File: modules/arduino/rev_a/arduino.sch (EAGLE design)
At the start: 45 parts, among them IC5 ATMEGA328P-20MU, J1 MODULE_GENERIC, J4 MICRO_USB_B_HIROSE_ZX62-B-5PA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, U3 ATMEGA8U2-MU, Y1 12 MHz, Y2 16MHz

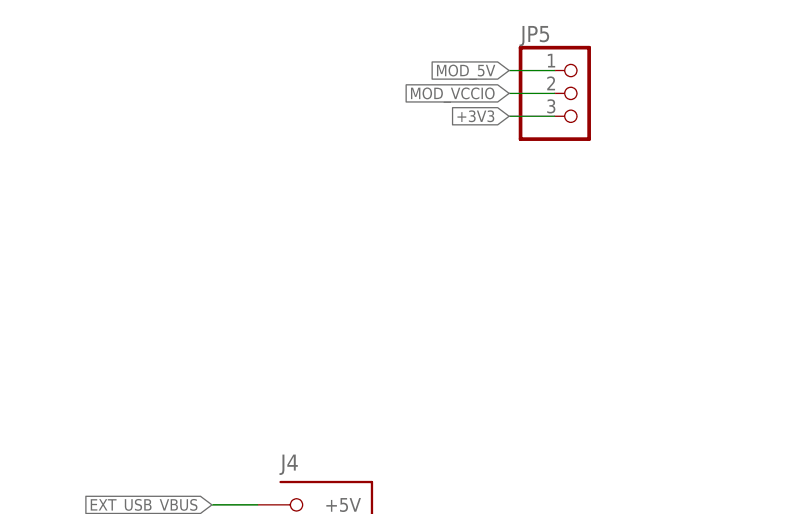
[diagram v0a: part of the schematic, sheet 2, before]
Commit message: Ardunio WIP
 - Add actual holes for signpost module mounts
 - Replace pin header with switch for IO voltage
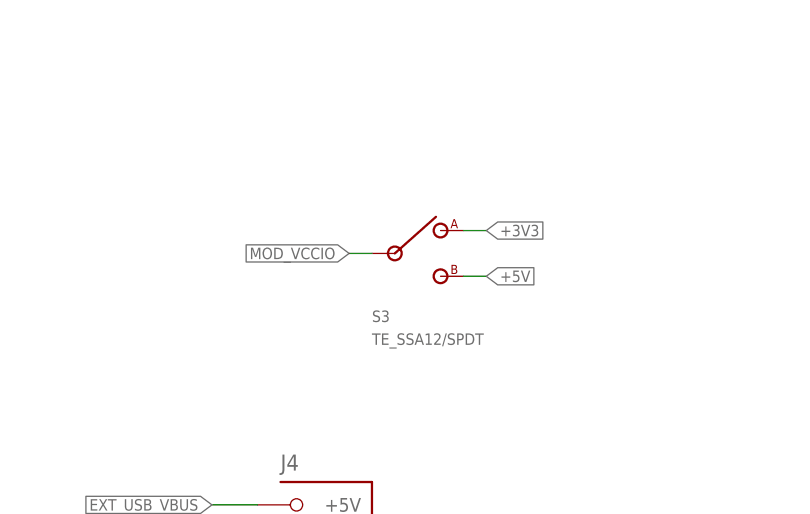
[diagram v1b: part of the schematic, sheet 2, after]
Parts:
- removed JP5: (no value), pinhead:PINHD-1X3
- added S3: TE_SSA12/SPDT, switches:TE_SSA12/SPDT
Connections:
- net +3V3: no longer JP5.3
- net +5V: now also S3.B
- net MOD_5V: no longer JP5.1
- net MOD_VCCIO: no longer JP5.2
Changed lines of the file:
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@@
 <part name="J1" library="signpost" deviceset="MODULE_GENERIC" device=""/>
 <part name="GND24" library="umich" deviceset="GND" device=""/>
-<part name="JP5" library="pinhead" deviceset="PINHD-1X3" device=""/>
 <part name="VR1" library="regulators" deviceset="TPS62086" device=""/>
 <part name="GND26" library="umich" deviceset="GND" device=""/>
@@
 <attribute name="DIGIKEY" value="535-9103-1-ND"/>
 </part>
+<part name="S3" library="switches" deviceset="TE_SSA12/SPDT" device=""/>
 </parts>
 <sheets>
@@
 <instance part="J1" gate="G$1" x="33.02" y="149.86"/>
 <instance part="GND24" gate="1" x="48.26" y="127"/>
-<instance part="JP5" gate="A" x="223.52" y="170.18"/>
 <instance part="VR1" gate="G$1" x="50.8" y="40.64"/>
 <instance part="GND26" gate="1" x="35.56" y="27.94"/>
@@
 <instance part="S1" gate="G$1" x="185.42" y="66.04"/>
 <instance part="GND28" gate="1" x="198.12" y="43.18"/>
+<instance part="S3" gate="G$1" x="203.2" y="152.4"/>
 </instances>
 <busses>
@@
 <net name="+3V3" class="0">
 <segment>
-<pinref part="JP5" gate="A" pin="3"/>
-<wire x1="215.9" y1="167.64" x2="220.98" y2="167.64" width="0.1524" layer="91"/>
-<label x="215.9" y="167.64" size="1.27" layer="95" rot="R180" xref="yes"/>
+<wire x1="213.36" y1="154.94" x2="210.82" y2="154.94" width="0.1524" layer="91"/>
+<label x="213.36" y="154.94" size="1.27" layer="95" xref="yes"/>
 </segment>
 <segment>
@@
 </segment>
 <segment>
-<pinref part="JP5" gate="A" pin="1"/>
-<wire x1="215.9" y1="172.72" x2="220.98" y2="172.72" width="0.1524" layer="91"/>
-<label x="215.9" y="172.72" size="1.27" layer="95" rot="R180" xref="yes"/>
-</segment>
-<segment>
 <pinref part="VR1" gate="G$1" pin="VIN"/>
 <wire x1="22.86" y1="45.72" x2="27.94" y2="45.72" width="0.1524" layer="91"/>
@@
 <net name="MOD_VCCIO" class="0">
 <segment>
-<pinref part="JP5" gate="A" pin="2"/>
-<wire x1="215.9" y1="170.18" x2="220.98" y2="170.18" width="0.1524" layer="91"/>
-<label x="215.9" y="170.18" size="1.27" layer="95" rot="R180" xref="yes"/>
+<wire x1="198.12" y1="152.4" x2="200.66" y2="152.4" width="0.1524" layer="91"/>
+<label x="198.12" y="152.4" size="1.27" layer="95" rot="R180" xref="yes"/>
 </segment>
 <segment>
@@
 <pinref part="D2" gate="G$1" pin="CATHODE"/>
 </segment>
-</net>
+<segment>
+<pinref part="S3" gate="G$1" pin="B"/>
+<wire x1="213.36" y1="149.86" x2="210.82" y2="149.86" width="0.1524" layer="91"/>
+<label x="213.36" y="149.86" size="1.27" layer="95" xref="yes"/>
+</segment>
+</net>

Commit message: Add Digikey attributes for Arduino MCUs
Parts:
- IC5: DIGIKEY (none) -> ATMEGA328P-MU-ND
- U3: DIGIKEY (none) -> ATMEGA8U2-MURCT-ND
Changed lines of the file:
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@@
 <part name="L" library="led" deviceset="LED" device="CHIP-LED0805" value="YELLOW"/>
 <part name="GND17" library="supply1" deviceset="GND" device=""/>
-<part name="U3" library="atmel" deviceset="ATMEGA8U2-MU" device=""/>
+<part name="U3" library="atmel" deviceset="ATMEGA8U2-MU" device="">
+<attribute name="DIGIKEY" value="ATMEGA8U2-MURCT-ND"/>
+</part>
 <part name="C5" library="SmartPrj" deviceset="C-EU" device="0603-RND" value="100n"/>
 <part name="ICSP1" library="pinhead" deviceset="PINHD-2X3" device="" value="ICSP"/>
@@
 <part name="GND8" library="supply1" deviceset="GND" device=""/>
 <part name="JP2" library="pinhead" deviceset="PINHD-2X2" device=""/>
-<part name="IC5" library="idii" deviceset="MEGA8" device="-MI" value="ATMEGA328P-20MU"/>
+<part name="IC5" library="idii" deviceset="MEGA8" device="-MI" value="ATMEGA328P-20MU">
+<attribute name="DIGIKEY" value="ATMEGA328P-MU-ND"/>
+</part>
 <part name="GND15" library="supply1" deviceset="GND" device=""/>
 <part name="FRAME1" library="lab11-frames" deviceset="LETTER_L_UMICH" device=""/>
@@
 <instance part="L" gate="G$1" x="287.02" y="116.84" rot="R90"/>
 <instance part="GND17" gate="1" x="299.72" y="116.84" rot="R90"/>
-<instance part="U3" gate="G$1" x="119.38" y="53.34"/>
+<instance part="U3" gate="G$1" x="119.38" y="53.34">
+<attribute name="DIGIKEY" x="119.38" y="53.34" size="1.27" layer="96" align="top-left" display="off"/>
+</instance>
 <instance part="C5" gate="G$1" x="180.34" y="81.28" rot="R90"/>
 <instance part="ICSP1" gate="A" x="60.96" y="99.06"/>
@@
 <attribute name="NAME" x="217.17" y="76.835" size="1.778" layer="95"/>
 <attribute name="VALUE" x="217.805" y="14.605" size="1.778" layer="96"/>
+<attribute name="DIGIKEY" x="233.68" y="48.26" size="1.27" layer="96" align="top-left" display="off"/>
 </instance>
 <instance part="GND15" gate="1" x="167.64" y="45.72"/>

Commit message: Not pretty but it's something
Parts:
- removed L1: BLM21, wuerth-elektronik:WE-CBF_0805
- removed Z1, Z2: PGB1010604, varistor:VARISTORCN0603
- added D1: DIODE, passives:DIODE
- added J2: (no value), jumper:SJ
- added LOGO1: UMICH_SOLID_MEDIUM, logos:UMICH_SOLID_MEDIUM
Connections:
- net N$7 renamed VR_IND_SW
- removed net USHIELD: L1.2, Z1.2, Z2.2
- net +3V3: now also S3.A
- net +5V: now also C10.1, D1.CATHODE, VR1.EN, VR1.VIN
- net ARD_USB_D+: now also RN3B.2; no longer RN3D.2, Z1.1
- net ARD_USB_D-: no longer Z2.1
- net ARD_USB_GND: no longer GROUND.2, L1.1
- net ARD_USB_VBUS: no longer D2.ANODE
- net EXT_USB_GND: now also GROUND.1
- net EXT_USB_VBUS: now also D2.ANODE
- net GND: now also GROUND.2; no longer GROUND.1
- net MOD_5V: now also D1.ANODE; no longer C10.1, VR1.EN, VR1.VIN
- net MOD_IN: now also J2.1
- net MOD_VCCIO: now also S3.IN
- net RD+: now also RN3B.1; no longer RN3D.1
- net RESET: now also J2.2
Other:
- note added: "RN3D to RN3B (routing)"
- note added: "Remove shield ESD circuitry"
- moved on the sheet: D2, RN3B, RN3D

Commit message: Arduino: WIP, I should commit more frequently :(
The primary change in this commit is to extend the 3.3V/5V selection to the whole
board. The nice observation is that the two MCUs are 2.7-5.5 and 1.8-5.5 VCC tolerant,
so can do run-time selection of core voltage with a little bit of careful design. This
lets the seinduino look either like a Due (3.3V) or a Uno (5V).

The next mission is to replace that reset trigger circuit with a one-shot so that we
aren't cooking 5mA all the time.
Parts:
- removed ICSP1: ICSP, pinhead:PINHD-2X3
- removed RN3: 22R, resistor-dil:4R-NCAY16
- added C1, C13, C2, C3: 100nF, passives:CAPACITOR0603_CAP
- added J3: ICSP_PROG, pinhead:PINHD-2X3
- added JP1: (no value), pinhead:PINHD-1X2
- added R4, R5: 22Ω, passives:RESISTOR-HIGH_SPEED0402
- added U1, U2: ADG3304, chips:ADG3304
- C7: value 100n -> 100nF
- C8: value 1u -> 1uF
- renumbered IC5 to U4, ICSP to J6, JP2 to J5
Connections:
- removed net EXT_USB_ID: J4.ID
- removed net MISO2: ICSP1.1, U3.(PD0/MISO/PCINT3)PB3
- removed net MOD_VCCIO: J1.VCCIO, S3.IN
- removed net MOSI2: ICSP1.4, U3.(PDI/MOSI/PCINT2)PB2
- removed net RD+: RN3B.1, U3.D+
- removed net RD-: RN3A.1, U3.D-
- removed net RESET2: ICSP1.5, RN1C.2, U3.RESET(PC1/DW)
- removed net SCK2: ICSP1.3, U3.(SCLK/PCINT1)PB1
- new net ARD_USB_D+_TERM: R5.P$1, U3.D+
- new net ARD_USB_D-_TERM: R4.P$1, U3.D-
- new net MISO_PROG: U1.A1, U3.(PD0/MISO/PCINT3)PB3
- new net MISO_PROG_SHIFTED: J3.1, U1.Y1
- new net MISO_SHIFTED: J6.1, U2.Y1
- new net MOSI_PROG: U1.A2, U3.(PDI/MOSI/PCINT2)PB2
- new net MOSI_PROG_SHIFTED: J3.4, U1.Y2
- new net MOSI_SHIFTED: J6.4, U2.Y2
- new net RESET_PROG: RN1C.2, U1.A4, U3.RESET(PC1/DW)
- new net RESET_PROG_SHIFTED: J3.5, U1.Y4
- new net RESET_SHIFTED: J6.5, U2.Y4
- new net SCK_PROG: U1.A3, U3.(SCLK/PCINT1)PB1
- new net SCK_PROG_SHIFTED: J3.3, U1.Y3
- new net SCK_SHIFTED: J6.3, U2.Y3
- new net VCC: C13.2, C2.2, C6.2, C7.1, J1.VCCIO, RN1C.1, RN1D.2, S3.IN, U1.EN, U1.VCC_A, U2.EN, U2.VCC_A, U3.AVCC, U3.VCC, U4.AVCC, U4.VCC@1, U4.VCC@2
- net +5V: now also C1.1, C3.1, J3.2, U1.VCC_Y, U2.VCC_Y; no longer C6.2, C7.1, ICSP1.2, RN1C.1, RN1D.2, U3.AVCC, U3.VCC, U4.AVCC, U4.VCC@1, U4.VCC@2
- net AD4: now also JP1.2
- net AD5: now also JP1.1
- net ARD_USB_D+: now also R5.P$2; no longer RN3B.2
- net ARD_USB_D-: now also R4.P$2; no longer RN3A.2
- net GND: now also C1.2, C13.1, C2.1, C3.2, J3.6, U1.GND, U2.GND; no longer ICSP1.6
- net MISO: now also U2.A1; no longer J6.1
- net MOSI: now also U2.A2; no longer J6.4
- net RESET: now also U2.A4; no longer J6.5
- net SCK: now also U2.A3; no longer J6.3
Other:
- note added: "AD4 = SDA"
- note added: "AD5 = SCL"
- note added: "Add missing extra SCL/SDA headers"
- note added: "Cautionary level conversion on the programming headers"
- note added: "Other Stuff:"
- note added: "Rename parts consistently"
- note added: "Replace RN3 array with discretes"
- note added: "Replace nets with labels where I just couldn't stand it any more"
- note added: "Update design to support either 3.3 or 5V for VCC"
- note added: "VCC Selection - Chooses core voltage for all MCUs - Chooses I/O voltage for all I/O lines - NOTE: Arduino ICSP header is always at +5V regardless of selection - Should match Due at 3.3V and Uno at 5V"
- note added: "http://forum.arduino.cc/index.php?topic=136595.0"
- note removed: "RN3D to RN3B (routing)"
- moved on the sheet: C4, C7, C8, F1, L, ON, POWER, RN1C, RN1D, RN2A, RN4C, RN4D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

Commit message: arudino: add reset network
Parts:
- removed J2, RESET-EN: (no value), jumper:SJ
- added C14, C15: 100nF, passives:CAPACITOR0603_CAP
- added R6: 10kΩ, passives:RESISTOR0603_RES
- added RESET-PROG-EN, RESET-SIGN-EN: (no value), jumper:SJ
- added U5: 74LVC2G00DC, chips:74LVC2G00DC
- added U6: SN74LVC1G123DCUR, chips:SN74LVC1G123DCUR
- C5: value 100n -> 100nF; device SmartPrj:C-EU0603-RND -> passives:CAPACITOR0603_CAP
- RN1: DIGIKEY (none) -> CAY16-103J4GLFCT-ND
- RN3: DIGIKEY (none) -> CAY16-102J4GLFCT-ND
- renumbered RN4 to RN3
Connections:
- removed net DTR: C5.1, RN2D.1, U3.(CTS/HWB/AIN6/TO/INT7)PD7
- new net DTR_PROG: RESET-PROG-EN.1, U3.(CTS/HWB/AIN6/TO/INT7)PD7
- new net N$10: RESET-SIGN-EN.2, RN1B.2, U5G$1.B
- new net N$13: U5G$2.A, U5G$2.B, U6.Q
- new net N$7: C5.2, RN1C.1, U6.C_EX
- new net N$8: U5G$1.Y, U6.!A
- new net N$9: RESET-PROG-EN.2, RN1A.2, U5G$1.A
- net GND: now also C14.1, C15.1, RN1C.2, U5G$3.GND, U6.GND; no longer RN2D.2
- net MOD_IN: now also RESET-SIGN-EN.1; no longer J2.1
- net RESET: now also RN1D.2, U5G$2.Y; no longer C5.2, J2.2, RESET-EN.1, RESET-EN.2, RN1D.1
- net RESET_PROG: now also R6.1; no longer RN1C.2
- net VCC: now also C14.2, C15.2, C5.1, R6.2, RN1A.1, RN1B.1, RN1D.1, U5G$3.VCC, U6.!CLR, U6.B, U6.R/C_EX, U6.VCC; no longer RN1C.1, RN1D.2
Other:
- note added: "1 ms pulse"
- note added: "Arduino uses serial DTR to trigger reset, with semantics of falling edge on DTR line results in negative pulse for reset"
- note added: "Replace reset (see right)"
- note added: "Reset Network"
- moved on the sheet: RN1C, RN1D

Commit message: Seinduino routed
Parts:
- removed RN2, RN3: 1K, resistor-dil:4R-NCAY16
- added C16: 100nF, passives:CAPACITOR0603_CAP
- added R10, R11, R12, R7, R8: 1kΩ, passives:RESISTOR0603_RES
- added R9: 470Ω, passives:RESISTOR0603_RES
- C4, C6: value 100n -> 100nF; device SmartPrj:C-EU0603-RND -> passives:CAPACITOR0603_CAP
- C7: device SmartPrj:C-EU0603-RND -> passives:CAPACITOR0603_CAP
- U1: value ADG3304 -> ATMEGA8U2-MU; device chips:ADG3304 -> atmel:ATMEGA8U2-MU; DIGIKEY (none) -> ATMEGA8U2-MURCT-ND
- U2: value ADG3304 -> ATMEGA328P-20MU; device chips:ADG3304 -> idii:MEGA8-MI; DIGIKEY (none) -> ATMEGA328P-MU-ND
- U3: value ATMEGA8U2-MU -> ADG3304; device atmel:ATMEGA8U2-MU -> chips:ADG3304; DIGIKEY ATMEGA8U2-MURCT-ND -> (none)
- U4: value ATMEGA328P-20MU -> ADG3304; device idii:MEGA8-MI -> chips:ADG3304; DIGIKEY ATMEGA328P-MU-ND -> (none)
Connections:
- removed net N$10: RESET-SIGN-EN.2, RN1B.2, U5G$1.B
- removed net N$9: RESET-PROG-EN.2, RN1A.2, U5G$1.A
- net +5V: now also R7.2, R8.2, R9.1, U3.VCC_Y, U4.VCC_Y; no longer RN2B.1, RN2C.1, RN3C.1, RN3D.1, U1.VCC_Y, U2.VCC_Y
- net AD0: now also U2.PC0(ADC0); no longer U4.PC0(ADC0)
- net AD1: now also U2.PC1(ADC1); no longer U4.PC1(ADC1)
- net AD2: now also U2.PC2(ADC2); no longer U4.PC2(ADC2)
- net AD3: now also U2.PC3(ADC3); no longer U4.PC3(ADC3)
- net AD4: now also U2.PC4(ADC4/SDA); no longer U4.PC4(ADC4/SDA)
- net AD5: now also U2.PC5(ADC5/SCL); no longer U4.PC5(ADC5/SCL)
- net ARD_USB_D+_TERM: now also U1.D+; no longer U3.D+
- net ARD_USB_D-_TERM: now also U1.D-; no longer U3.D-
- net ARD_USB_GND: now also U1.UGND; no longer U3.UGND
- net AREF: now also U2.AREF; no longer U4.AREF
- net DTR_PROG: now also RESET-PROG-EN.2, RN1A.2, U1.(CTS/HWB/AIN6/TO/INT7)PD7, U5G$1.A; no longer U3.(CTS/HWB/AIN6/TO/INT7)PD7
- net GND: now also C16.2, C6.2, RN1D.2, U1.PAD, U2.AGND, U2.GND@1, U2.GND@2, U4.GND; no longer C6.1, RN1C.2, U2.GND, U3.PAD, U4.AGND, U4.GND@1, U4.GND@2
- net IO0: now also R11.2, U2.PD0(RXD); no longer RN3B.1, U4.PD0(RXD)
- net IO1: now also R12.2, U2.PD1(TXD); no longer RN3A.1, U4.PD1(TXD)
- net IO2: now also U2.PD2(INT0); no longer U4.PD2(INT0)
- net IO3: now also U2.PD3(INT1); no longer U4.PD3(INT1)
- net IO4: now also U2.PD4(XCK/T0); no longer U4.PD4(XCK/T0)
- net IO5: now also U2.PD5(T1); no longer U4.PD5(T1)
- net IO6: now also U2.PD6(AIN0); no longer U4.PD6(AIN0)
- net IO7: now also U2.PD7(AIN1); no longer U4.PD7(AIN1)
- net IO8: now also U2.PB0(ICP); no longer U4.PB0(ICP)
- net IO9: now also U2.PB1(OC1A); no longer U4.PB1(OC1A)
- net M8RXD: now also R11.1, U1.(TXD1/INT3)PD3; no longer RN3B.2, U3.(TXD1/INT3)PD3
- net M8TXD: now also R12.1, U1.(RXD1/AIN1/INT2)PD2; no longer RN3A.2, U3.(RXD1/AIN1/INT2)PD2
- net MISO: now also U2.PB4(MISO), U3.A1; no longer U2.A1, U4.PB4(MISO)
- net MISO_PROG: now also U1.(PD0/MISO/PCINT3)PB3, U4.A3; no longer U1.A1, U3.(PD0/MISO/PCINT3)PB3
- net MISO_PROG_SHIFTED: now also U4.Y3; no longer U1.Y1
- net MISO_SHIFTED: now also U3.Y1; no longer U2.Y1
- net MOD_IN: now also RESET-SIGN-EN.2, RN1B.2, U5G$1.B
- net MOSI: now also U2.PB3(MOSI/OC2), U3.A2; no longer U2.A2, U4.PB3(MOSI/OC2)
- net MOSI_PROG: now also U1.(PDI/MOSI/PCINT2)PB2, U4.A2; no longer U1.A2, U3.(PDI/MOSI/PCINT2)PB2
- net MOSI_PROG_SHIFTED: now also U4.Y2; no longer U1.Y2
- net MOSI_SHIFTED: now also U3.Y2; no longer U2.Y2
- net N$1: now also R10.2; no longer RN2A.1
- net N$2: now also U1.(T1/PCINT4)PB4; no longer U3.(T1/PCINT4)PB4
- net N$3: now also R9.2; no longer RN3C.2, RN3D.2
- net N$35: now also R8.1; no longer RN2B.2
- net N$36: now also R7.1; no longer RN2C.2
- net N$4: now also U1.(PCINT5)PB5; no longer U3.(PCINT5)PB5
- net N$5: now also U1.(PCINT6)PB6; no longer U3.(PCINT6)PB6
- net N$6: now also U1.(PCINT7/OC0A/OC1C)PB7; no longer U3.(PCINT7/OC0A/OC1C)PB7
- net N$7: now also RN1D.1; no longer RN1C.1
- net RESET: now also RN1C.2, U2.PC6(/RESET), U3.A4; no longer RN1D.2, U2.A4, U4.PC6(/RESET)
- net RESET_PROG: now also U1.RESET(PC1/DW), U4.A4; no longer U1.A4, U3.RESET(PC1/DW)
- net RESET_PROG_SHIFTED: now also U4.Y4; no longer U1.Y4
- net RESET_SHIFTED: now also U3.Y4; no longer U2.Y4
- net RXLED: now also U1.(INT5/AIN3)PD4; no longer U3.(INT5/AIN3)PD4
- net SCK: now also R10.1, U2.PB5(SCK), U3.A3; no longer RN2A.2, U2.A3, U4.PB5(SCK)
- net SCK_PROG: now also U1.(SCLK/PCINT1)PB1, U4.A1; no longer U1.A3, U3.(SCLK/PCINT1)PB1
- net SCK_PROG_SHIFTED: now also U4.Y1; no longer U1.Y3
- net SCK_SHIFTED: now also U3.Y3; no longer U2.Y3
- net SS: now also U2.PB2(SS/OC1B); no longer U4.PB2(SS/OC1B)
- net TXLED: now also U1.(XCK/AIN4/PCINT12)PD5; no longer U3.(XCK/AIN4/PCINT12)PD5
- net USBVCC: now also U1.UVCC; no longer U3.UVCC
- net VCC: now also C16.1, C6.1, RN1C.1, U1.AVCC, U1.VCC, U2.AVCC, U2.VCC@1, U2.VCC@2, U3.EN, U3.VCC_A, U4.EN, U4.VCC_A; no longer C6.2, RN1D.1, U1.EN, U1.VCC_A, U2.EN, U2.VCC_A, U3.AVCC, U3.VCC, U4.AVCC, U4.VCC@1, U4.VCC@2
- net VUCAP: now also U1.UCAP; no longer U3.UCAP
- net XT1: now also U1.XTAL1; no longer U3.XTAL1
- net XT2: now also U1.XTAL2(PC0); no longer U3.XTAL2(PC0)
- net XTAL1: now also U2.PB6(XTAL1/TOSC1); no longer U4.PB6(XTAL1/TOSC1)
- net XTAL2: now also U2.PB7(XTAL2/TOSC2); no longer U4.PB7(XTAL2/TOSC2)
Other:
- note added: "Enable by default"
- note removed: "USB boot En"
- moved on the sheet: RESET-PROG-EN, RESET-SIGN-EN, RN1C, RN1D, RX, TX
